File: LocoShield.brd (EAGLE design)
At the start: 50 x 50 mm, 28 parts, among them J2 RJ12/6, J3 RJ12/6, Q1 2N3904, U1 LM393M, U2 LM317LCDR

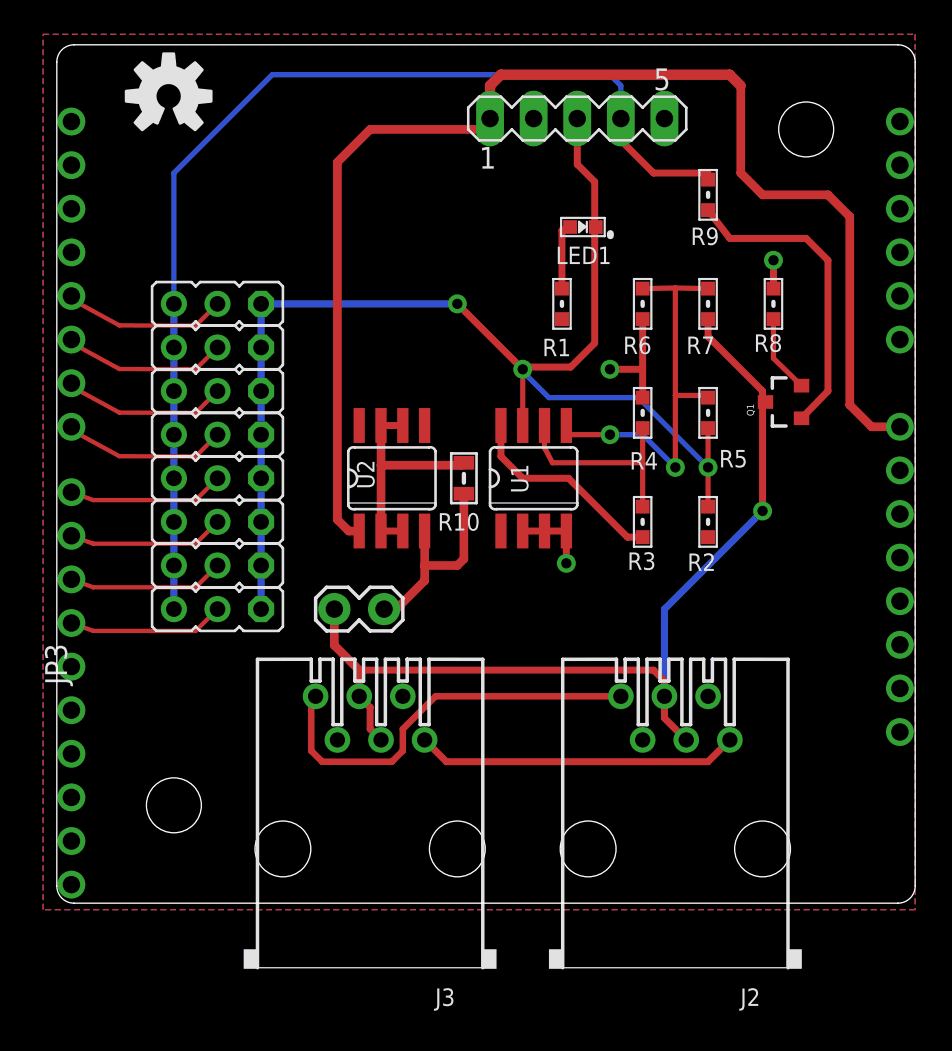
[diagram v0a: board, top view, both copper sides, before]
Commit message: moved away from shield form
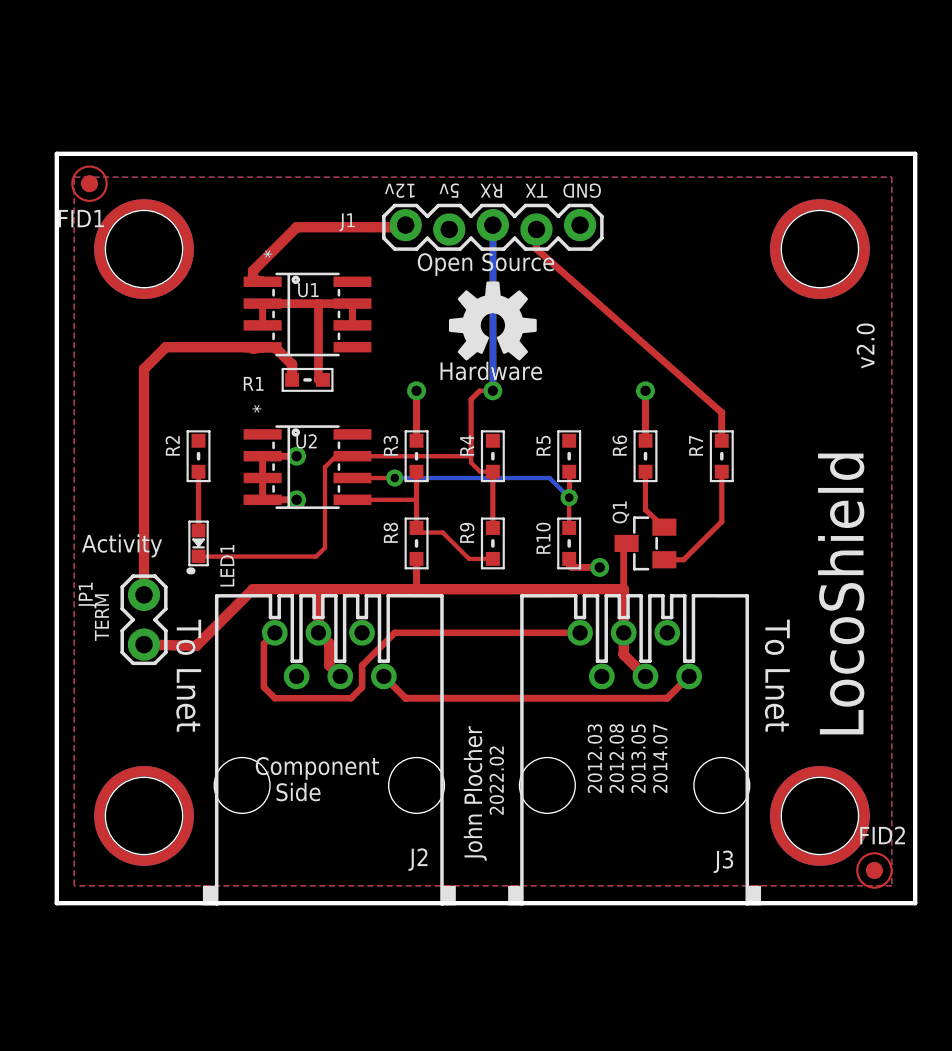
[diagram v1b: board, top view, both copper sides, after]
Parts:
- removed JP3: 0.100, MCP:1X02_LOCK
- removed JPD10, JPD11, JPD4, JPD5, JPD6, JPD7, JPD8, JPD9: 0.100, MCP:JP2
- removed SHIELD: ARDUINO_SHIELD, SPCoast:DUEMILANOVE_VIAS
- removed SV1: 0.100, con-lstb:MA05-1
- removed U$1: OSHW, SparkFun:OSHW-LOGO-M
- added FID1, FID2: FIDUCIAL, SPCoast:FIDUCIAL_1MM
- added H1, H2, H3, H4: MOUNTINGHOLEL, SPCoast:MOUNTINGHOLE-L
- added J1: 0.100, SPCoast:1X05_LOCK
- added JP1: 0.100, SPCoast:1X02_LOCK
- added U$3: OSHW, SPCoast:OSHW-LOGO-M
- Q1: device MCP:SOT23-3 -> SPCoast:SOT23
- R1: value 470R -> 82R
- R10: value 82R -> 39k; device SPCoast:0805-RES -> SPCoast:0603-RES
- R2: value 1k -> 470R
- R3: value 27k -> 150k
- R4: value 39k -> 1k
- R5: value 240k -> 27k
- R6: value 150k -> 47R
- R7: value 47k -> 4k7
- R8: value 47R -> 47k
- R9: value 4k7 -> 240k
- U1: value LM393M -> LM317LCDR; device MCP:SO08 -> SPCoast:SO08
- U2: value LM317LCDR -> LM393M; device MCP:SO08 -> SPCoast:SO08
- moved R2 29.9 mm to (8.26, 26.0), turned to 270 degrees
- moved LED1 29.0 mm to (8.26, 21.0), turned to 90 degrees
- moved R8 25.0 mm to (21.0, 21.0)
- moved R9 23.9 mm to (25.4, 21.0), turned to 90 degrees
- moved J2 20.5 mm to (15.9, 6.86)
- moved U1 16.3 mm to (14.6, 34.3), turned to 270 degrees
- moved J3 15.8 mm to (33.7, 6.86)
- moved R1 15.5 mm to (14.6, 30.5), turned to 180 degrees
- moved R3 13.7 mm to (21.0, 26.0), turned to 270 degrees
- moved Q1 11.5 mm to (34.3, 21.0), turned to 0 degrees
- moved R4 9.08 mm to (25.4, 26.0)
- moved R7 8.91 mm to (38.7, 26.0), turned to 270 degrees
- moved R6 8.88 mm to (34.3, 26.0)
- moved R5 8.47 mm to (29.8, 26.0)
- moved R10 7.21 mm to (29.8, 21.0), turned to 90 degrees
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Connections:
- removed net D10: JPD10.2, SHIELD.D10
- removed net D11: JPD11.2, SHIELD.D11
- removed net D4: JPD4.2, SHIELD.D4
- removed net D5: JPD5.2, SHIELD.D5
- removed net D6: JPD6.2, SHIELD.D6
- removed net D7: JPD7.2, SHIELD.D7
- removed net D8: JPD8.2, SHIELD.D8
- removed net D9: JPD9.2, SHIELD.D9
- net GND: now also J1.5, R10.1, R3.1, R6.2, U2.2, U2.3, U2.4; no longer R4.1, R6.1, R8.2, SHIELD.GND@0, SHIELD.GND@1, SHIELD.GND@2, SV1.5, U1.2, U1.3, U1.4
- net LNRX: now also J1.3, R4.2, R9.2, U2.7; no longer JPD10.1, JPD11.1, JPD4.1, JPD5.1, JPD6.1, JPD7.1, JPD8.1, JPD9.1, R2.2, R5.2, SV1.3, U1.7
- net LNTX: now also J1.4, R7.1; no longer JPD10.3, JPD11.3, JPD4.3, JPD5.3, JPD6.3, JPD7.3, JPD8.3, JPD9.3, R9.1, SV1.4
- net LOCONET: now also JP1.1, R8.1; no longer JP3.1, R7.1
- net N$1: now also R7.2; no longer R9.2
- net N$15: now also R2.2; no longer R1.2
- net N$2: now also R3.2, R8.2, R9.1, U2.5; no longer R5.1, R6.2, R7.2, U1.5
- net N$20: now also JP1.2, R1.2, U1.4; no longer JP3.2, R10.2, U2.4
- net N$5: now also R10.2, R5.2, U2.6; no longer R3.2, R4.2, U1.6
- net N$6: now also R6.1; no longer R8.1
- net V+: now also J1.1, U1.1; no longer SHIELD.VIN, SV1.1, U2.1
- net VCC: now also J1.2, R4.1, R5.1, U2.8; no longer R1.1, R3.1, SHIELD.5V, SV1.2, U1.8
- net VOUT: now also R1.1, U1.2, U1.3, U1.6, U1.7; no longer R10.1, U2.2, U2.3, U2.6, U2.7
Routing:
- net V+: track 76.3 -> 11.7 mm
- net LNTX: track 64.8 -> 17.2 mm
- net LNRX: track 74.6 -> 40.6 mm, vias 3 -> 1
- net N$20: track 12.2 -> 24.8 mm
- net VCC: track 12.0 -> 0.00 mm
- net LOCONET: track 56.6 -> 45.2 mm, vias 1 -> 0
- net N$2: track 23.8 -> 12.9 mm, vias 2 -> 0
- net N$1: track 18.2 -> 7.29 mm
- net D7: track 9.61 -> 0.00 mm
- net D6: track 9.61 -> 0.00 mm
- net D5: track 9.61 -> 0.00 mm
- net D4: track 9.61 -> 0.00 mm
- net D10: track 9.12 -> 0.00 mm
- net D8: track 9.12 -> 0.00 mm
- net D11: track 9.12 -> 0.00 mm
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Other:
- board size 50 x 50 mm -> 50 x 43.6 mm
- board text added: "2022.02"
- board text added: "J1"
- board text added: "J2"
- board text added: "J3"
- board text added: "JP1"
- board text added: "LED1"
- board text added: "Q1"
- board text added: "R1"
- board text added: "R10"
- board text added: "R2"
- board text added: "R3"
- board text added: "R4"
- board text added: "R5"
- board text added: "R6"
- board text added: "R7"
- board text added: "R8"
- board text added: "R9"
- board text added: "U1"
- board text added: "U2"
- board text added: "v2.0"
- board text removed: "10"
- board text removed: "5"
- board text removed: "6"
- board text removed: "7"
- board text removed: "8"
- board text removed: "9"
- board text removed: "D11"
- board text removed: "D4"
- board text removed: "D4=RX"
- board text removed: "D5=TX"
- board text removed: "D8=RX"
- board text removed: "D9=TX"
- board text removed: "LEO"
- board text removed: "UNO"
- board text removed: "v1.4"

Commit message: fixed silk layout
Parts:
- renumbered FID1 to FIDUL, FID2 to FIDLR
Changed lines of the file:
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@@
 <wire x1="1.6129" y1="37.529" x2="6.0579" y2="41.466" width="2.54" layer="52"/>
 <wire x1="38.3159" y1="1.207" x2="40.3479" y2="3.366" width="2.54" layer="52"/>
-<text x="11.5189" y="5.954" size="1.016" layer="21" font="vector" rot="SR0">Component
+<text x="11.5189" y="0.874" size="1.016" layer="21" font="vector" rot="SR0">Component
    Side</text>
 <text x="24.765" y="2.54" size="1.016" layer="21" font="vector" rot="SR90">John Plocher</text>
@@
 <elements>
 <element name="J3" library="SPCoast" package="RJ25-PANEL" value="RJ12/6" x="33.655" y="6.858" smashed="yes">
-<attribute name="NAME" x="39.497" y="3.048" size="1.016" layer="25" font="vector" rot="R180"/>
-<attribute name="VALUE" x="33.274" y="3.048" size="1.016" layer="27" font="vector" rot="R180"/>
+<attribute name="NAME" x="39.497" y="10.668" size="1.016" layer="25" font="vector" rot="R180"/>
+<attribute name="VALUE" x="37.084" y="5.588" size="1.016" layer="27" font="vector" rot="R180"/>
 <attribute name="OPL" value="none" x="33.655" y="6.858" size="1.778" layer="27" display="off"/>
 <attribute name="AMP" value="520250-3" x="33.655" y="6.858" size="1.778" layer="27" display="off"/>
 </element>
 <element name="J2" library="SPCoast" package="RJ25-PANEL" value="RJ12/6" x="15.875" y="6.858" smashed="yes">
-<attribute name="NAME" x="21.717" y="3.175" size="1.016" layer="25" font="vector" rot="R180"/>
-<attribute name="VALUE" x="15.367" y="3.175" size="1.016" layer="27" font="vector" rot="R180"/>
+<attribute name="NAME" x="21.717" y="10.795" size="1.016" layer="25" font="vector" rot="R180"/>
+<attribute name="VALUE" x="19.177" y="5.715" size="1.016" layer="27" font="vector" rot="R180"/>
 <attribute name="OPL" value="none" x="15.875" y="6.858" size="1.778" layer="27" display="off"/>
 <attribute name="AMP" value="520250-3" x="15.875" y="6.858" size="1.778" layer="27" display="off"/>
@@
 <attribute name="VALUE" x="32.385" y="41.275" size="0.8128" layer="27" rot="R270"/>
 </element>
-<element name="FID1" library="SPCoast" package="FIDUCIAL_1MM" value="FIDUCIAL" x="1.905" y="41.91"/>
-<element name="FID2" library="SPCoast" package="FIDUCIAL_1MM" value="FIDUCIAL" x="47.625" y="1.905" rot="R180"/>
+<element name="FIDUL" library="SPCoast" package="FIDUCIAL_1MM" value="FIDUCIAL" x="1.905" y="41.91" smashed="yes">
+<attribute name="NAME" x="3.175" y="41.91" size="1.016" layer="25"/>
+</element>
+<element name="FIDLR" library="SPCoast" package="FIDUCIAL_1MM" value="FIDUCIAL" x="47.625" y="1.905" smashed="yes" rot="R180">
+<attribute name="NAME" x="46.355" y="1.905" size="1.016" layer="25" rot="R180"/>
+</element>
 </elements>
 <signals>

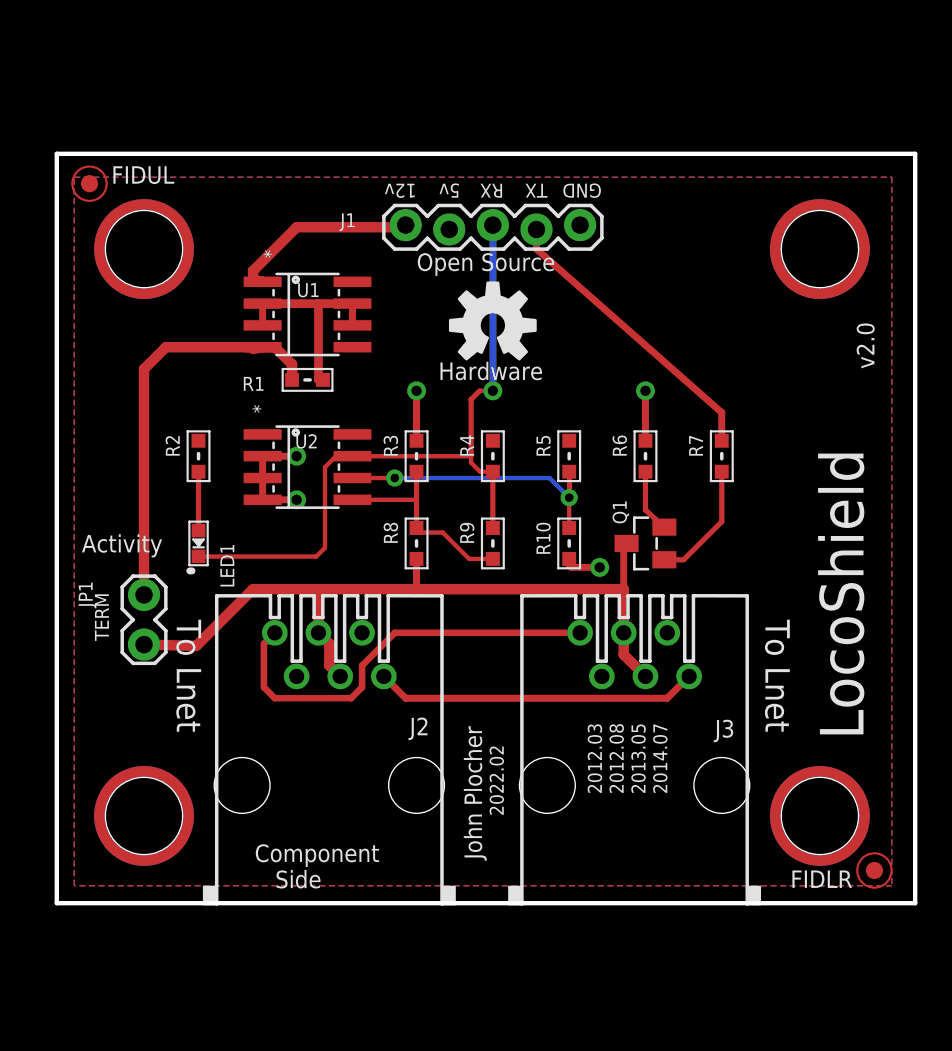
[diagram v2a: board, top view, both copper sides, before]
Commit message: added tooling for JLC
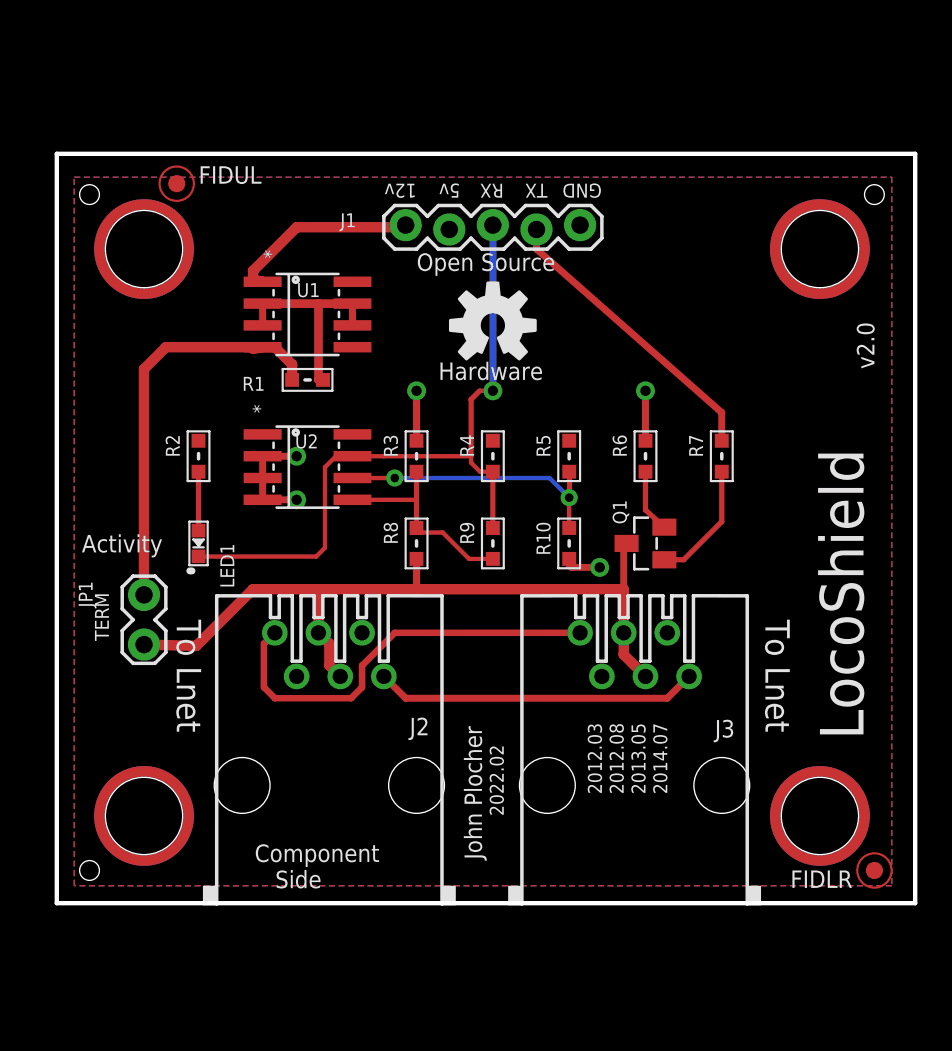
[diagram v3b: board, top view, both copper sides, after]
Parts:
- added MT1, MT2, MT3: tool, SPCoast:MOUNTINGHOLE-TOOL
- H1, H2, H3, H4: value MOUNTINGHOLEL -> (none)
- LED1: value B -> Blue
- moved FIDUL 5.08 mm to (6.99, 41.9)
